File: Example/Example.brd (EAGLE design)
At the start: 86 x 54 mm, 12 parts, among them IC1 LM555D, J1 UX60-MB-5S8, Q2 BSS806N, SW1 MFS101D-6-Z

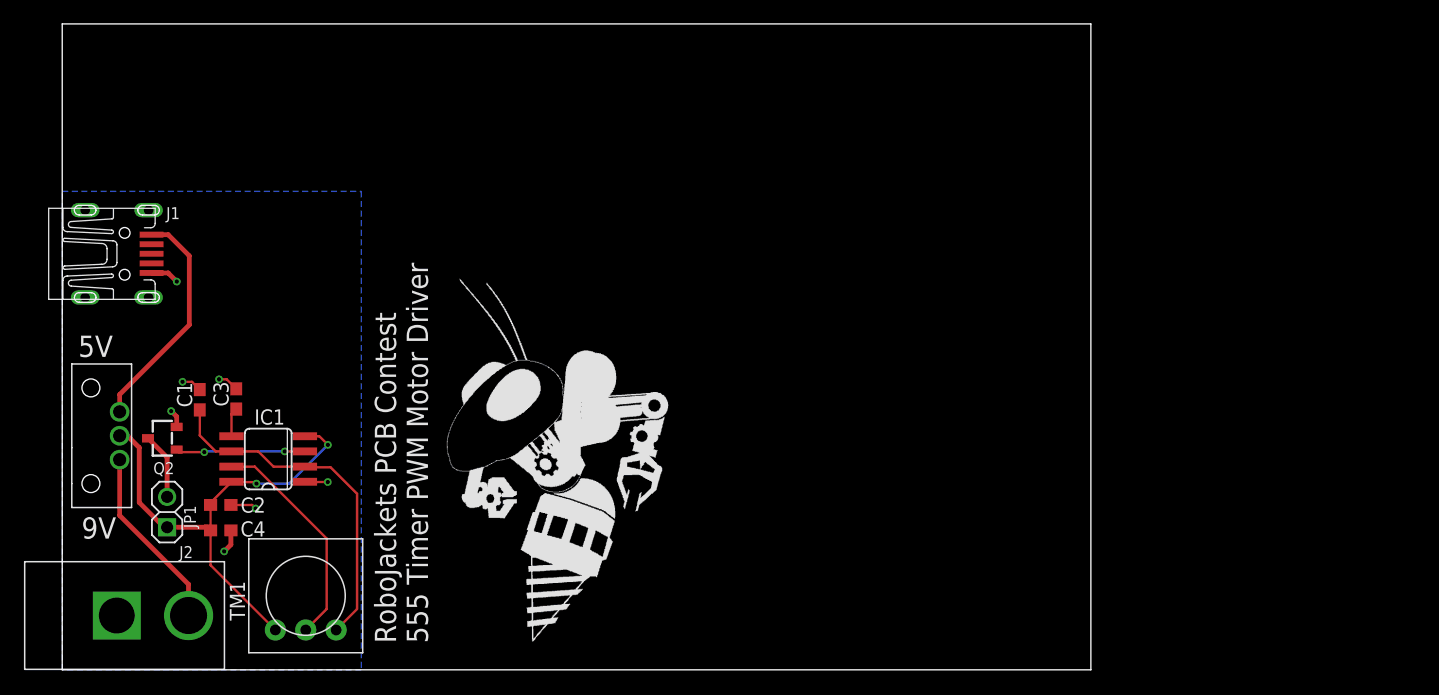
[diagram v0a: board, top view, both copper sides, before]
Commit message: Made footprints for motors, battery case, and guiding spring
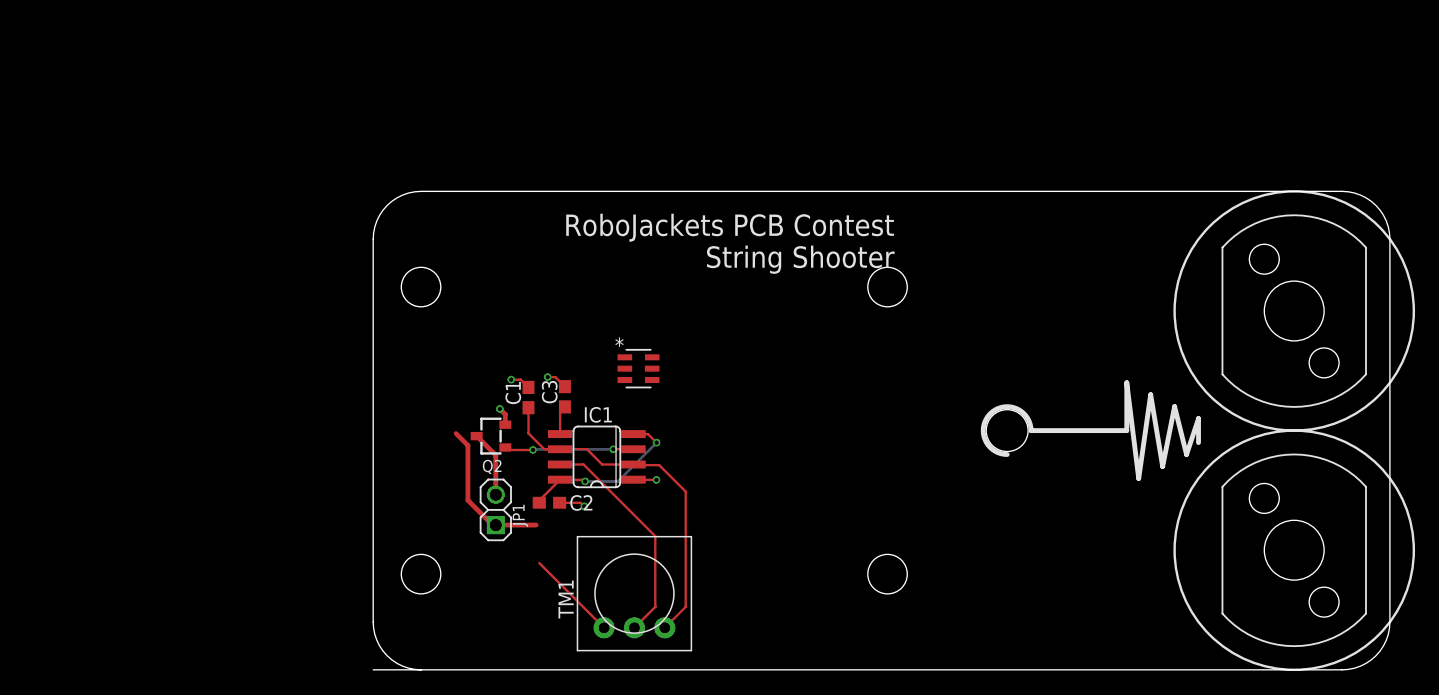
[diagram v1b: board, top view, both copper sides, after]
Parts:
- removed C4: 10uF, rcl:C0603
- removed J1: UX60-MB-5S8, RoboJackets-Connectors:UX60-MB-5S8
- removed J2: (no value), RoboJackets-Connectors:PJ-037A
- removed SW1: MFS101D-6-Z, Example:MFS101D-6-Z
- added U$1: BATTERY-DEVICE, battery-stringshooter-holder-18650:BATTERY-CASE
- added U$3, U$4: LITTLE-MOTOR, motor-stringshooter:DC_MOTOR
- added U1: LT6700CS6-2, LT6700CS6-2:TSOT-23_S6
- U$2: value (none) -> SPRING-CONTACT; device RoboJackets-Aesthetics:ROBOBUZZ_1.4X -> battery-contact-AA:SPRING-CONTACT
- moved U$2 37.9 mm to (75.0, 15.0)
- moved C3 27.5 mm to (42.0, 22.8)
- moved Q2 27.5 mm to (35.9, 19.5)
- moved TM1 27.5 mm to (47.8, 6.37)
- moved IC1 27.5 mm to (44.7, 17.8)
- moved JP1 27.5 mm to (36.2, 13.4)
- moved C1 27.5 mm to (39.0, 22.8)
- moved C2 27.5 mm to (40.7, 14.0)
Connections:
- removed net N$4: J1.1, SW1.3
- removed net N$6: J2.P$2, SW1.1
- new net VS: U1.5
- net +9V: no longer C4.1, SW1.2
- net GND: now also U1.2; no longer C4.2, J1.5, J2.P$1
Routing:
- net N$4: track 19.3 -> 0.00 mm
- net N$6: track 15.4 -> 0.00 mm
- net +9V: track 40.6 -> 34.5 mm
- net GND: track 13.5 -> 9.08 mm, vias 7 -> 5
- removed copper zone on layer 16, net GND
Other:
- board size 86 x 54 mm -> 85 x 40 mm
- board text added: "RoboJackets PCB Contest String Shooter"
- board text removed: "5V"
- board text removed: "9V"
- board text removed: "RoboJackets PCB Contest 555 Timer PWM Motor Driver"
